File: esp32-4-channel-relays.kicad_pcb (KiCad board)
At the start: 2 copper layers, 86.4 x 86.6 mm, 63 parts, among them J1 Relay-1, J2 Relay-2, J3 Relay-3, J4 Relay-4, K1 SRD-05VDC-SL-C, K2 SRD-05VDC-SL-C, K3 SRD-05VDC-SL-C, K4 SRD-05VDC-SL-C, Q1 MBT3904DW1, Q2 BC547A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

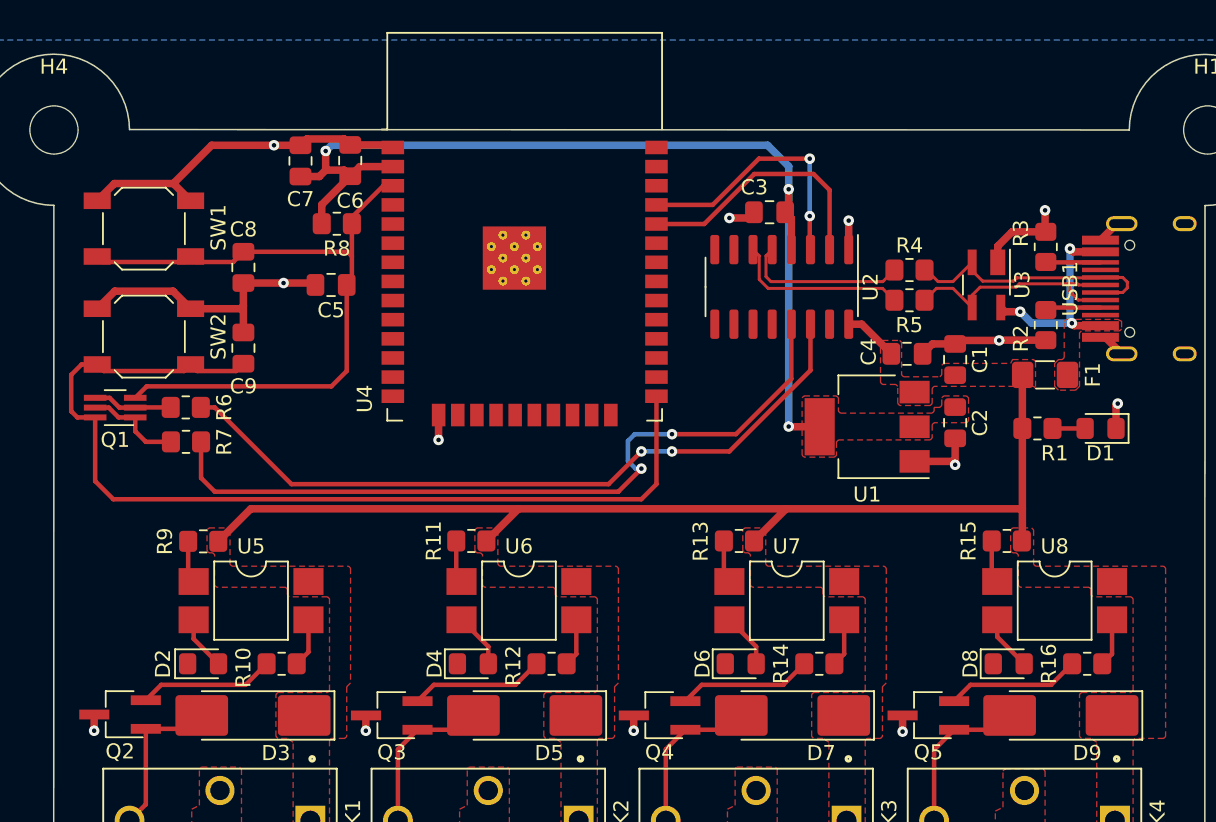
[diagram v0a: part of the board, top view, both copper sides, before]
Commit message: Routing relays to esp32 and design rules check
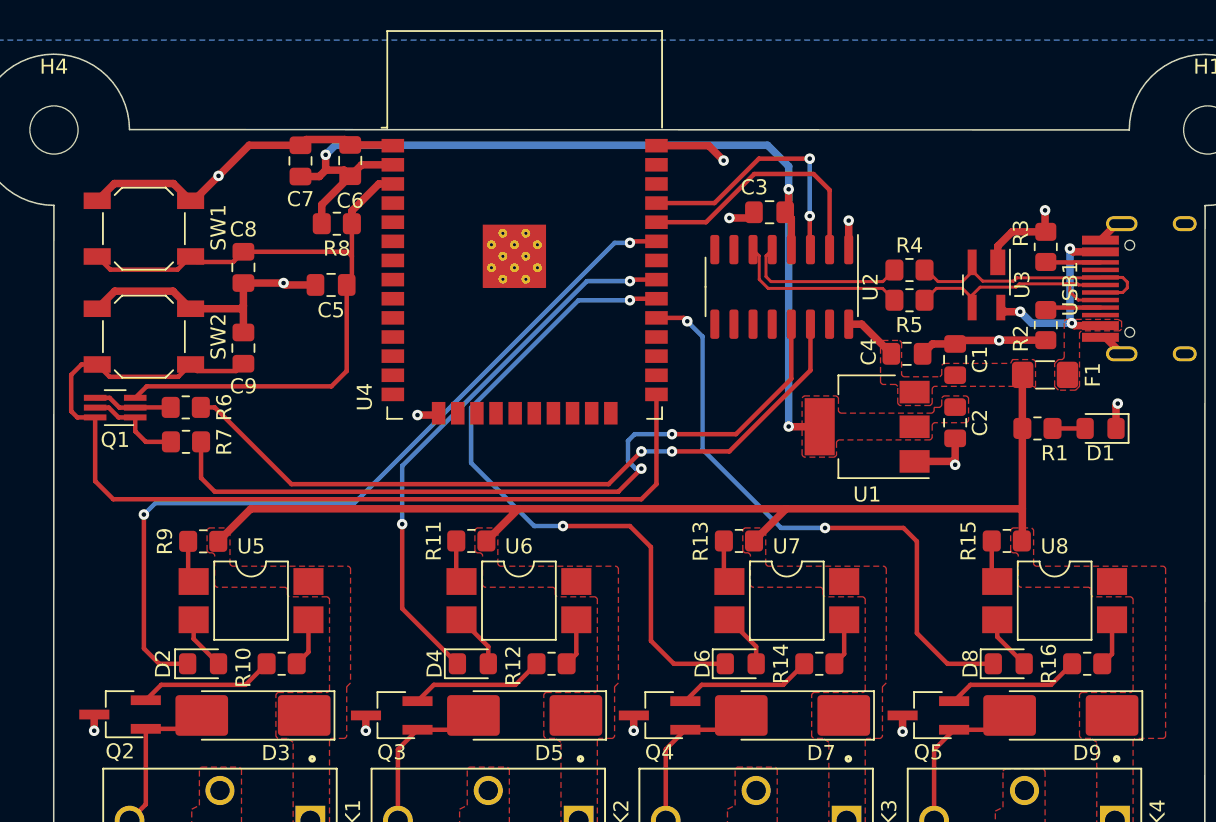
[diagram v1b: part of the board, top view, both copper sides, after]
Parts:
- moved U4 0.12 mm to (157.9, 62.9)
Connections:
- D2 pad 1: /IO_23 -> /IO_21
- D4 pad 1: /IO_22 -> /IO_19
- D6 pad 1: /IO_19 -> /IO_18
- D8 pad 1: /IO_21 -> /IO_5
- U4 pad 29: unconnected-(U4-IO5-Pad29) -> /IO_5
- U4 pad 30: unconnected-(U4-IO18-Pad30) -> /IO_18
- U4 pad 36: /IO_22 -> unconnected-(U4-IO22-Pad36)
- U4 pad 37: /IO_23 -> unconnected-(U4-IO23-Pad37)
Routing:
- net /IO_21: track 0.00 -> 53.7 mm, vias 0 -> 2
- net /IO_18: track 0.00 -> 45.0 mm, vias 0 -> 2
- net /IO_5: track 0.00 -> 39.8 mm, vias 0 -> 2
- net /IO_19: track 0.00 -> 36.7 mm, vias 0 -> 2
- net GND: track 76.2 -> 78.8 mm, vias 13 -> 14
- net Net-(D7-A): track 10.7 -> 9.33 mm
- net Net-(D9-A): track 10.7 -> 9.31 mm
- net Net-(D5-A): track 10.7 -> 9.33 mm
- net /RESET: track 46.5 -> 45.2 mm
- net Net-(D3-A): track 10.6 -> 9.36 mm
- net Net-(R9-Pad1): track 2.82 -> 2.30 mm
- net Net-(R15-Pad1): track 2.84 -> 2.33 mm
- net Net-(R13-Pad1): track 2.84 -> 2.33 mm

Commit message: Design rules check and lock components
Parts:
- moved R16 27.3 mm to (173.6, 105.7)
- moved C9 27.3 mm to (117.6, 84.7)
- moved R6 27.3 mm to (113.8, 88.6)
- moved R7 27.3 mm to (113.8, 90.9)
- moved R9 27.3 mm to (114.9, 97.5)
- moved C7 27.3 mm to (121.4, 72.3)
- moved C8 27.3 mm to (117.6, 79.3)
- moved J1 27.3 mm to (110.9, 139.7)
- moved R3 27.3 mm to (170.8, 78.0)
- moved C1 27.3 mm to (164.8, 85.5)
- moved C4 27.3 mm to (161.6, 85.1)
- moved D2 27.3 mm to (114.9, 105.7)
- moved D3 27.3 mm to (118.2, 109.1)
- moved D4 27.3 mm to (132.8, 105.7)
- moved D5 27.3 mm to (136.3, 109.1)
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
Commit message: Add Labels for relays, switch button and LED power indicator
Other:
- board text added: "locked"
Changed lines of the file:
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@@
         (effects (font (size 1 1) (thickness 0.15)))
     )
-    (fp_text value "Relay-1" (at 5.08 5.66) (layer "F.Fab")
+    (fp_text value "Relay-1" (at 5.08 5.66) (layer "F.Fab") hide
         (effects (font (size 1 1) (thickness 0.15)))
     )
@@
     (property "ki_keywords" "mounting hole")
     (attr exclude_from_pos_files)
-    (fp_text reference "H2" (at 0 -4.2) (layer "F.SilkS")
+    (fp_text reference "H2" (at 0 -4.2) (layer "F.SilkS") hide
         (effects (font (size 1 1) (thickness 0.15)))
     )
-    (fp_text value "MountingHole" (at 0 4.2) (layer "F.Fab")
+    (fp_text value "MountingHole" (at 0 4.2) (layer "F.Fab") hide
         (effects (font (size 1 1) (thickness 0.15)))
     )
@@
     (property "ki_keywords" "mounting hole")
     (attr exclude_from_pos_files)
-    (fp_text reference "H3" (at 0 -4.2) (layer "F.SilkS")
+    (fp_text reference "H3" (at 0 -4.2) (layer "F.SilkS") hide
         (effects (font (size 1 1) (thickness 0.15)))
     )
-    (fp_text value "MountingHole" (at 0 4.2) (layer "F.Fab")
+    (fp_text value "MountingHole" (at 0 4.2) (layer "F.Fab") hide
         (effects (font (size 1 1) (thickness 0.15)))
     )
@@
     (property "ki_keywords" "mounting hole")
     (attr exclude_from_pos_files)
-    (fp_text reference "H4" (at 0 -4.2) (layer "F.SilkS")
+    (fp_text reference "H4" (at 0 -4.2) (layer "F.SilkS") hide
         (effects (font (size 1 1) (thickness 0.15)))
     )
-    (fp_text value "MountingHole" (at 0 4.2) (layer "F.Fab")
+    (fp_text value "MountingHole" (at 0 4.2) (layer "F.Fab") hide
         (effects (font (size 1 1) (thickness 0.15)))
     )
@@
         (effects (font (size 1 1) (thickness 0.15)))
     )
-    (fp_text value "YELLOW_LED" (at -2.667 0 90) (layer "F.Fab")
+    (fp_text value "YELLOW_LED" (at -2.667 0 90) (layer "F.Fab") hide
         (effects (font (size 1 1) (thickness 0.15)))
     )
@@
         (effects (font (size 1 1) (thickness 0.15)))
     )
-    (fp_text value "Relay-4" (at 5.08 5.66) (layer "F.Fab")
+    (fp_text value "Relay-4" (at 5.08 5.66) (layer "F.Fab") hide
         (effects (font (size 1 1) (thickness 0.15)))
     )
@@
         (effects (font (size 1 1) (thickness 0.15)))
     )
-    (fp_text value "Relay-2" (at 5.08 5.66) (layer "F.Fab")
+    (fp_text value "Relay-2" (at 5.08 5.66) (layer "F.Fab") hide
         (effects (font (size 1 1) (thickness 0.15)))
     )
@@
         (effects (font (size 1 1) (thickness 0.15)))
     )
-    (fp_text value "HRO-TYPE-C-31-M-12" (at 0 1.15 90) (layer "Dwgs.User")
+    (fp_text value "HRO-TYPE-C-31-M-12" (at -2.292183 -2.581671 90) (layer "Dwgs.User")
         (effects (font (size 1 1) (thickness 0.15)))
     )
@@
         (effects (font (size 1 1) (thickness 0.15)))
     )
-    (fp_text value "Relay-3" (at 5.08 5.66) (layer "F.Fab")
+    (fp_text value "Relay-3" (at 5.08 5.66) (layer "F.Fab") hide
         (effects (font (size 1 1) (thickness 0.15)))
     )
@@
     (property "ki_keywords" "mounting hole")
     (attr exclude_from_pos_files)
-    (fp_text reference "H1" (at 0 -4.2) (layer "F.SilkS")
+    (fp_text reference "H1" (at 0 -4.2) (layer "F.SilkS") hide
         (effects (font (size 1 1) (thickness 0.15)))
     )
-    (fp_text value "MountingHole" (at 0 4.2) (layer "F.Fab")
+    (fp_text value "MountingHole" (at 0 4.2) (layer "F.Fab") hide
         (effects (font (size 1 1) (thickness 0.15)))
     )
@@
   (gr_line locked (start 181.414235 75.2433) (end 181.391933 141.804738)
     (stroke (width 0.1) (type default)) (layer "Edge.Cuts"))
+  (gr_text locked "NO" (at 163.322 145.923) (layer "F.SilkS")
+    (effects (font (size 0.8 0.8) (thickness 0.2) bold) (justify left bottom))
+  )
+  (gr_text locked "Channel-1" (at 107.696 142.24 90) (layer "F.SilkS")
+    (effects (font (size 0.8 0.8) (thickness 0.2) bold) (justify left bottom))
+  )
+  (gr_text locked "RESET" (at 105.56875 75.40625 270) (layer "F.SilkS")
+    (effects (font (size 0.8 0.8) (thickness 0.2) bold) (justify left bottom))
+  )
+  (gr_text locked "PWR" (at 177.546 91.313 90) (layer "F.SilkS")
+    (effects (font (size 0.8 0.8) (thickness 0.2) bold) (justify left bottom))
+  )
+  (gr_text locked "NO" (at 145.415 145.923) (layer "F.SilkS")
+    (effects (font (size 0.8 0.8) (thickness 0.2) bold) (justify left bottom))
+  )
+  (gr_text locked "COM" (at 168.275 145.923) (layer "F.SilkS")
+    (effects (font (size 0.8 0.8) (thickness 0.2) bold) (justify left bottom))
+  )
+  (gr_text locked "COM" (at 132.715 145.923) (layer "F.SilkS")
+    (effects (font (size 0.8 0.8) (thickness 0.2) bold) (justify left bottom))
+  )
+  (gr_text locked "NC" (at 173.736 145.923) (layer "F.SilkS")
+    (effects (font (size 0.8 0.8) (thickness 0.2) bold) (justify left bottom))
+  )
+  (gr_text locked "Channel-4" (at 161.036 142.264067 90) (layer "F.SilkS")
+    (effects (font (size 0.8 0.8) (thickness 0.2) bold) (justify left bottom))
+  )
+  (gr_text locked "NC" (at 138.176 145.923) (layer "F.SilkS")
+    (effects (font (size 0.8 0.8) (thickness 0.2) bold) (justify left bottom))
+  )
+  (gr_text locked "COM" (at 114.808 145.923) (layer "F.SilkS")
+    (effects (font (size 0.8 0.8) (thickness 0.2) bold) (justify left bottom))
+  )
+  (gr_text locked "Channel-2" (at 125.476 142.24 90) (layer "F.SilkS")
+    (effects (font (size 0.8 0.8) (thickness 0.2) bold) (justify left bottom))
+  )
+  (gr_text locked "NO" (at 127.762 145.923) (layer "F.SilkS")
+    (effects (font (size 0.8 0.8) (thickness 0.2) bold) (justify left bottom))
+  )
+  (gr_text locked "Channel-3" (at 143.256 142.264067 90) (layer "F.SilkS")
+    (effects (font (size 0.8 0.8) (thickness 0.2) bold) (justify left bottom))
+  )
+  (gr_text locked "COM" (at 150.368 145.923) (layer "F.SilkS")
+    (effects (font (size 0.8 0.8) (thickness 0.2) bold) (justify left bottom))
+  )
+  (gr_text locked "NO" (at 109.855 145.923) (layer "F.SilkS")
+    (effects (font (size 0.8 0.8) (thickness 0.2) bold) (justify left bottom))
+  )
+  (gr_text locked "BOOT" (at 105.537 82.296 270) (layer "F.SilkS")
+    (effects (font (size 0.8 0.8) (thickness 0.2) bold) (justify left bottom))
+  )
+  (gr_text locked "NC" (at 120.269 145.923) (layer "F.SilkS")
+    (effects (font (size 0.8 0.8) (thickness 0.2) bold) (justify left bottom))
+  )
+  (gr_text locked "NC" (at 155.829 145.923) (layer "F.SilkS")
+    (effects (font (size 0.8 0.8) (thickness 0.2) bold) (justify left bottom))
+  )
   (segment locked (start 115.916671 97.531817) (end 118.075671 95.372817) (width 0.5) (layer "F.Cu") (net 1))
   (segment locked (start 133.712671 97.506417) (end 135.846271 95.372817) (width 0.5) (layer "F.Cu") (net 1))
